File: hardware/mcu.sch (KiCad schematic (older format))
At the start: 27 parts, among them P1 CONN_01X17, SW1 SPST, SW2 SPST, U1 MCP2551-I/SN, U2 LPC11C14, U3 MCP2515_TSSOP, U4 MCP2551-I/SN

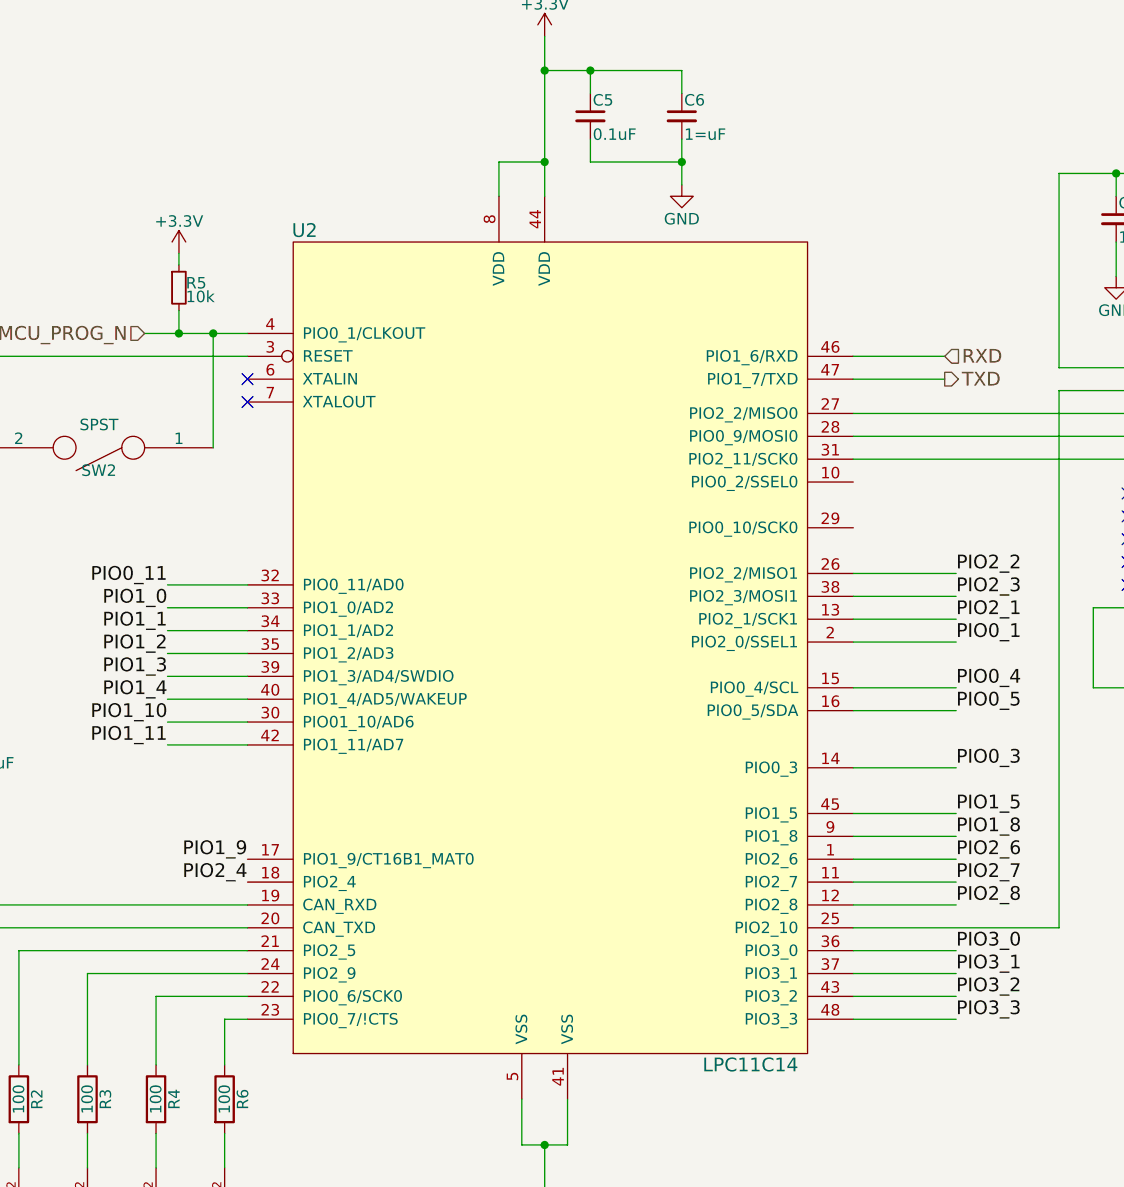
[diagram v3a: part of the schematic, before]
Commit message: Fixed some warnings (like unconnected pins)
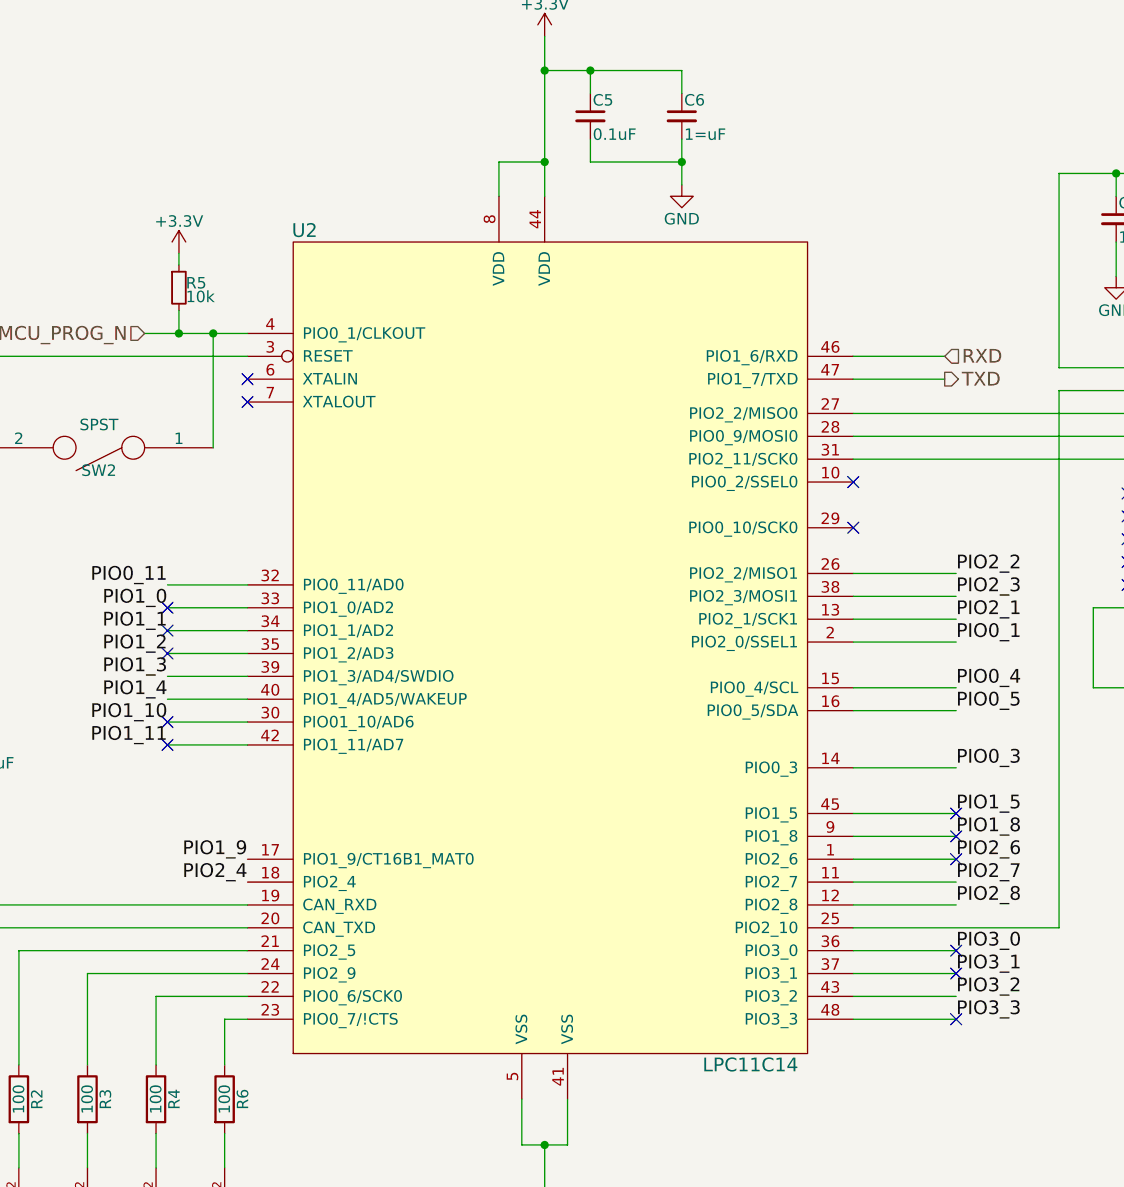
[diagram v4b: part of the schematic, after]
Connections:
- no-connect marks 14 -> 27
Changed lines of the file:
@@
 	4600 1850 4600 1700
 Wire Wire Line
-	4800 1700 4600 1700
+	4600 1700 4800 1700
 Wire Wire Line
 	4800 1150 4800 1850
@@
 Wire Wire Line
 	6150 5150 6600 5150
-Wire Wire Line
-	6150 5250 6600 5250
 Wire Wire Line
 	6150 5350 6600 5350
@@
 $EndComp
 $Comp
-L +3.3V #PWR?
+L +3.3V #PWR029
 U 1 1 56969D5D
 P 9050 4250
-F 0 "#PWR?" H 9050 4100 50  0001 C CNN
+F 0 "#PWR029" H 9050 4100 50  0001 C CNN
 F 1 "+3.3V" H 9050 4390 50  0000 C CNN
 F 2 "" H 9050 4250 50  0000 C CNN
@@
 Wire Wire Line
 	9050 4600 9050 4250
+NoConn ~ 6150 3100
+NoConn ~ 6150 3300
+Wire Wire Line
+	6600 5250 6150 5250
+NoConn ~ 6600 4550
+NoConn ~ 6600 4650
+NoConn ~ 6600 4750
+NoConn ~ 6600 5150
+NoConn ~ 6600 5250
+NoConn ~ 6600 5450
+NoConn ~ 3150 3650
+NoConn ~ 3150 3750
+NoConn ~ 3150 3850
+NoConn ~ 3150 4150
+NoConn ~ 3150 4250
 $EndSCHEMATC
